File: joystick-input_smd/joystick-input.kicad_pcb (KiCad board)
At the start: 2 copper layers, 53.3 x 29 mm, 18 parts, among them J1 Conn_01x18, J2 Conn_02x14_Odd_Even

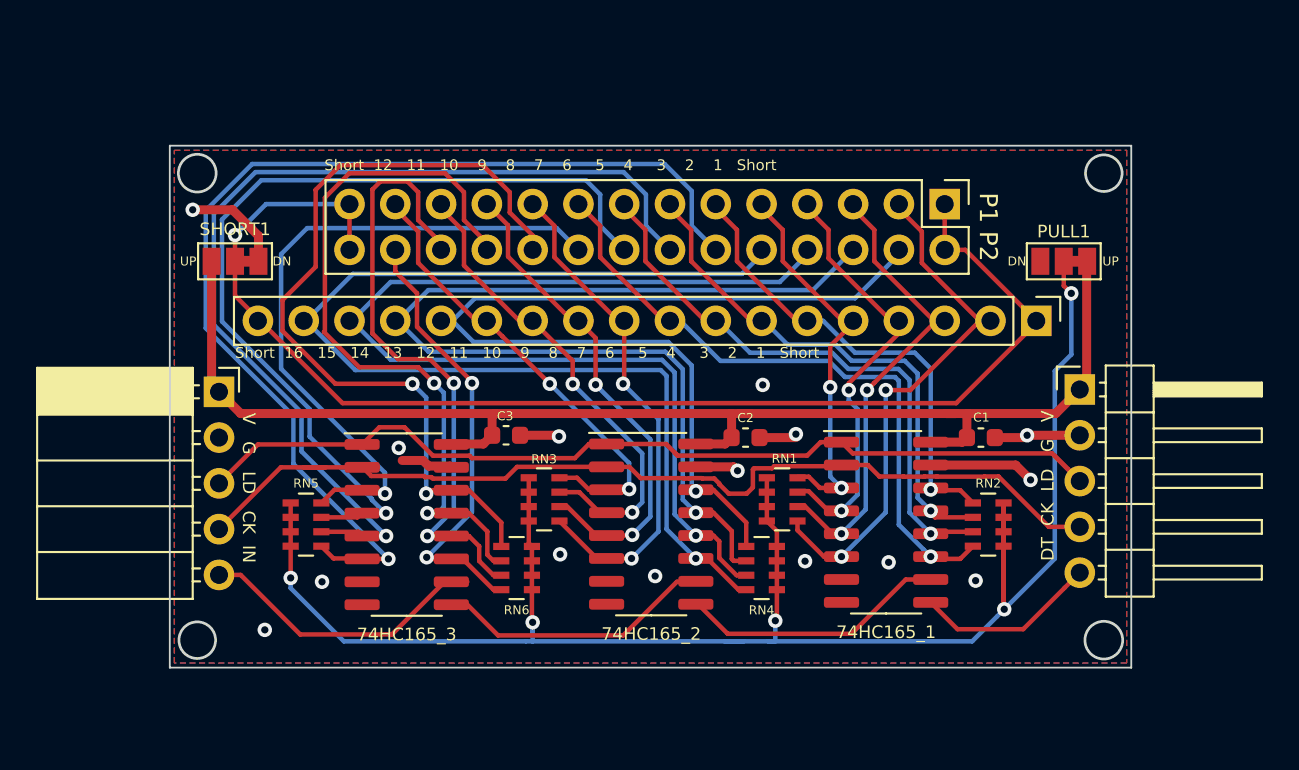
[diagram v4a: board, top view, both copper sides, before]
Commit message: joystick 입력 보드 smd 버전 문서 보강
Signed-off-by: Ju, Gyeong-min <jcmh74@gmail.com>
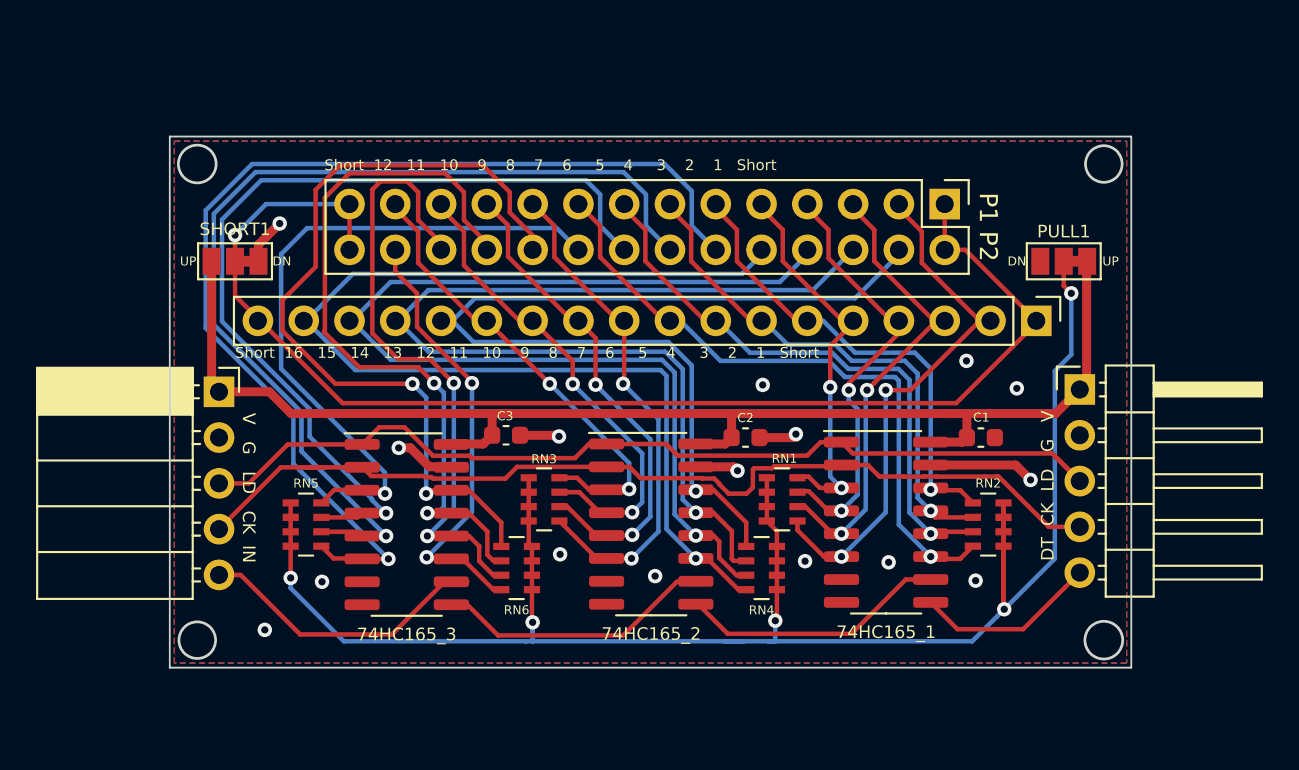
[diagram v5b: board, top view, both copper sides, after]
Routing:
- net GND: track 25.9 -> 18.6 mm, vias 15 -> 16
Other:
- board size 53.3 x 29 mm -> 53.3 x 29.5 mm

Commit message: joystick 입력보드 smd 타입 배선 최적화
Signed-off-by: Ju, Gyeong-min <jcmh74@gmail.com>
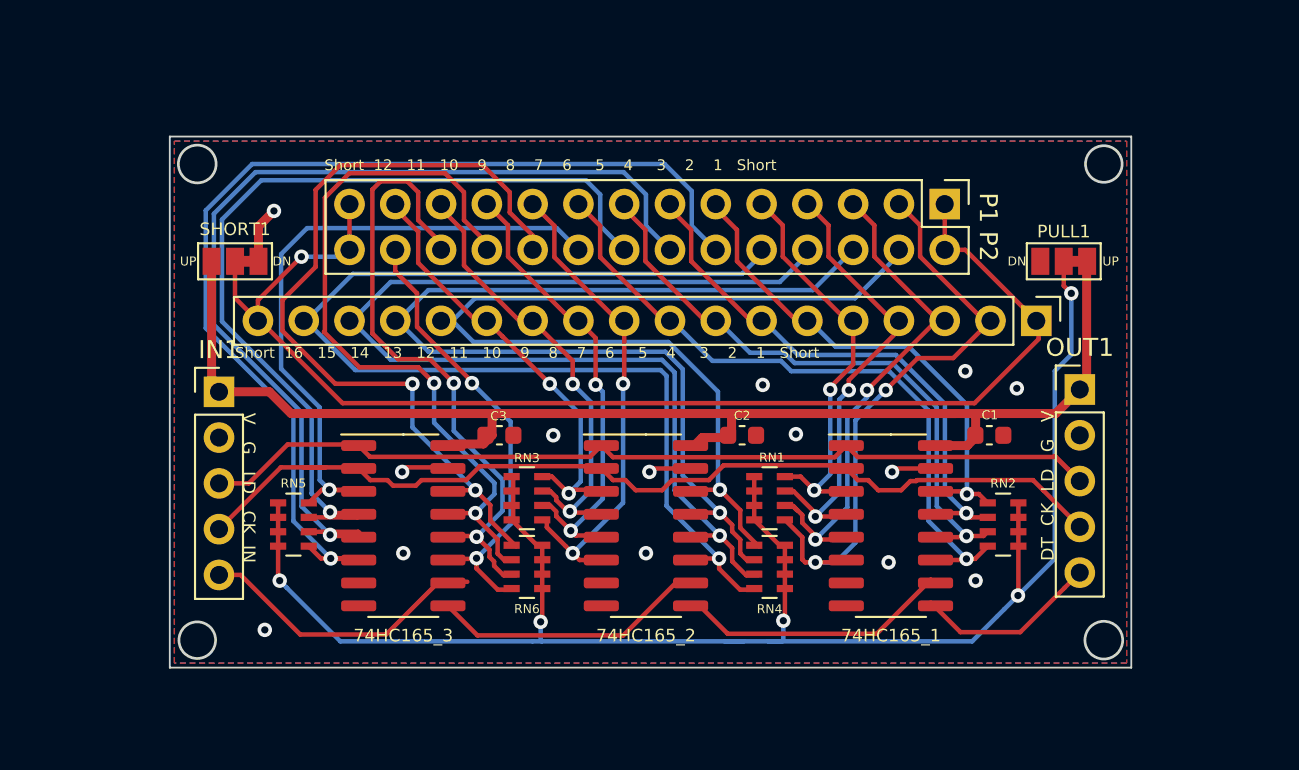
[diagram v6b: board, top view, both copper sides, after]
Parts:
- IN1: footprint Connector_PinSocket_2.54mm:PinSocket_1x05_P2.54mm_Horizontal -> Connector_PinHeader_2.54mm:PinHeader_1x05_P2.54mm_Vertical
- OUT1: footprint Connector_PinHeader_2.54mm:PinHeader_1x05_P2.54mm_Horizontal -> Connector_PinHeader_2.54mm:PinHeader_1x05_P2.54mm_Vertical
- moved RN3 0.95 mm to (131.6, 87.8)
- moved RN2 0.83 mm to (158.1, 89.3)
- moved RN1 0.70 mm to (145.1, 87.8)
- moved RN5 0.70 mm to (118.7, 89.3)
- moved RN6 0.58 mm to (131.6, 91.6)
- moved C1 0.49 mm to (157.3, 84.3)
- moved RN4 0.45 mm to (145.1, 91.6)
- moved C3 0.37 mm to (130.1, 84.3)
- moved 74HC165_1 0.33 mm to (151.8, 89.3)
- moved 74HC165_2 0.31 mm to (138.2, 89.3)
- moved C2 0.23 mm to (143.6, 84.3)
- moved 74HC165_3 0.20 mm to (124.8, 89.3)
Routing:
- net GND: track 18.6 -> 10.7 mm, vias 16 -> 14
- net /PULL: track 99.9 -> 94.9 mm
- net /C_P1_UP: track 28.7 -> 33.2 mm
- net /C_P1_DOWN: track 26.0 -> 29.7 mm
- net /C_P1_LEFT: track 23.6 -> 25.7 mm
- net /C_P1_SELECT: track 28.9 -> 30.6 mm
- net /C_P1_A: track 32.2 -> 33.9 mm
- net /C_P1_L: track 26.6 -> 25.1 mm
- net /C_P2_RIGHT: track 62.4 -> 64.0 mm
- net /C_P1_Y: track 27.4 -> 25.9 mm
- net /C_P1_START: track 26.0 -> 27.6 mm
- net /C_P1_B: track 35.9 -> 37.4 mm
- net /LOAD: track 53.2 -> 51.8 mm
- net /C_P1_X: track 28.3 -> 27.0 mm
- net /C_P1_RIGHT: track 21.6 -> 22.8 mm
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
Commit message: joystick smd 타입 배선 최적화
Signed-off-by: Ju, Gyeong-min <jcmh74@gmail.com>
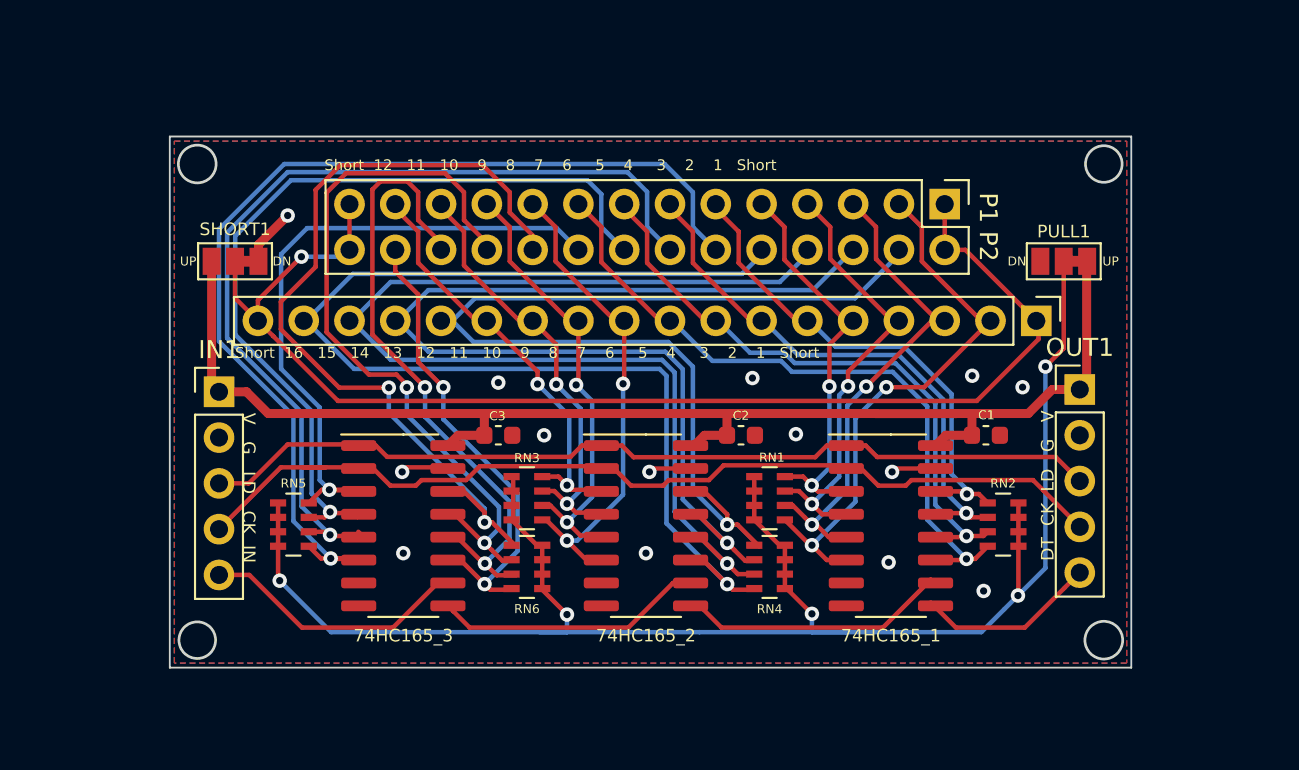
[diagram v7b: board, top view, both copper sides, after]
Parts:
- moved C1 0.19 mm to (157.1, 84.3)
- moved C2 0.06 mm to (143.5, 84.3)
- moved C3 0.06 mm to (130.0, 84.3)
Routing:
- net /C_P2_SELECT: track 54.4 -> 51.4 mm
- net /C_P2_A: track 49.4 -> 46.5 mm
- net /C_P2_UP: track 53.5 -> 55.8 mm
- net /C_P1_UP: track 33.2 -> 31.0 mm
- net /D_IN: track 16.9 -> 15.2 mm
- net /C_P2_START: track 59.6 -> 58.0 mm
- net /C_P1_DOWN: track 29.7 -> 28.2 mm
- net /C_P2_LEFT: track 60.8 -> 62.2 mm
- net /C_P2_RIGHT: track 64.0 -> 65.2 mm
- net /C_P2_DOWN: track 57.9 -> 59.1 mm
- net /C_P2_R: track 25.2 -> 26.4 mm
- net /C_P1_R: track 24.5 -> 23.4 mm
- net /LOAD: track 51.8 -> 50.7 mm
- net /C_P2_X: track 45.4 -> 46.4 mm
- net /C_P1_L: track 25.1 -> 24.1 mm
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
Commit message: joystick smd pcb 배선 최적화
Signed-off-by: Ju, Gyeong-min <jcmh74@gmail.com>
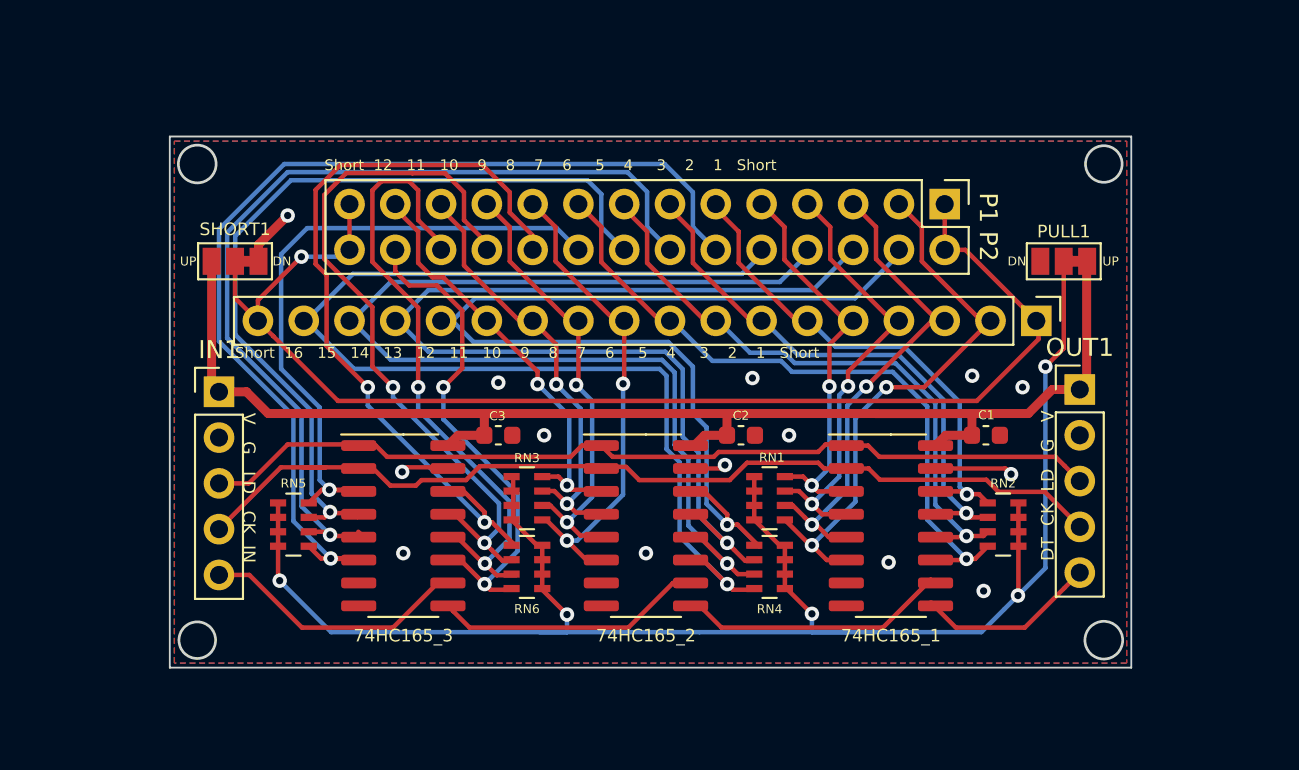
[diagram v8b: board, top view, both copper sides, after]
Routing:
- net /C_P2_X: track 46.4 -> 43.2 mm
- net /C_P2_R: track 26.4 -> 28.2 mm
- net GND: track 10.7 -> 12.2 mm
- net /C_P2_Y: track 41.5 -> 40.8 mm
